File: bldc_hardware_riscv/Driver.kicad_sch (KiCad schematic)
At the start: 95 parts, among them Q1 Q_NMOS_GDS, Q2 Q_NMOS_GDS, Q3 Q_NMOS_GDS, Q4 Q_NMOS_GDS, Q5 Q_NMOS_GDS, Q6 Q_NMOS_GDS, U101 MAX9919, U102 MAX9919, U103 MAX9919, U2 XL1509-3.3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

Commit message: First release to PCB manufacture
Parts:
- U101, U102, U103: value MAX9919 -> (none); footprint BLDC_Library:HSOP-8-1EP_3.9x4.9mm_P1.27mm_EP2.3x2.3mm -> (none)
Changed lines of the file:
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@@
       (effects (font (size 1.27 1.27)) (justify left))
     )
-    (property "Value" "MAX9919" (id 1) (at 212.09 97.79 0)
-      (effects (font (size 1.27 1.27)) (justify left))
-    )
-    (property "Footprint" "BLDC_Library:HSOP-8-1EP_3.9x4.9mm_P1.27mm_EP2.3x2.3mm" (id 2) (at 203.2 99.695 0)
+    (property "Value" "" (id 1) (at 212.09 97.79 0)
+      (effects (font (size 1.27 1.27)) (justify left))
+    )
+    (property "Footprint" "" (id 2) (at 203.2 99.695 0)
       (effects (font (size 1.27 1.27)) hide)
     )
@@
     (pin "2")
   )
-  (symbol (lib_id "BLDC_Library:MAX9919") (at 205.105 31.115 0) (unit 1)
+  (symbol (lib_name "MAX9919_1") (lib_id "BLDC_Library:MAX9919") (at 205.105 31.115 0) (unit 1)
     (in_bom yes) (on_board yes)
     (property "Reference" "U103" (id 0) (at 212.09 31.75 0)
       (effects (font (size 1.27 1.27)) (justify left))
     )
-    (property "Value" "MAX9919" (id 1) (at 212.09 29.21 0)
-      (effects (font (size 1.27 1.27)) (justify left))
-    )
-    (property "Footprint" "BLDC_Library:HSOP-8-1EP_3.9x4.9mm_P1.27mm_EP2.3x2.3mm" (id 2) (at 203.2 31.115 0)
+    (property "Value" "" (id 1) (at 212.09 29.21 0)
+      (effects (font (size 1.27 1.27)) (justify left))
+    )
+    (property "Footprint" "" (id 2) (at 203.2 31.115 0)
       (effects (font (size 1.27 1.27)) hide)
     )
@@
     (pin "2")
   )
-  (symbol (lib_id "BLDC_Library:MAX9919") (at 205.105 65.405 0) (unit 1)
+  (symbol (lib_name "MAX9919_2") (lib_id "BLDC_Library:MAX9919") (at 205.105 65.405 0) (unit 1)
     (in_bom yes) (on_board yes)
     (property "Reference" "U102" (id 0) (at 212.09 66.04 0)
       (effects (font (size 1.27 1.27)) (justify left))
     )
-    (property "Value" "MAX9919" (id 1) (at 212.09 63.5 0)
-      (effects (font (size 1.27 1.27)) (justify left))
-    )
-    (property "Footprint" "BLDC_Library:HSOP-8-1EP_3.9x4.9mm_P1.27mm_EP2.3x2.3mm" (id 2) (at 203.2 65.405 0)
-      (effects (font (size 1.27 1.27)) hide)
-    )
+    (property "Value" "" (id 1) (at 212.09 63.5 0)
+      (effects (font (size 1.27 1.27)) (justify left))
+    )
+    (property "Footprint" "" (id 2) (at 203.2 65.405 0)
+      (effects (font (size 1.27 1.27)) hide)
+    )

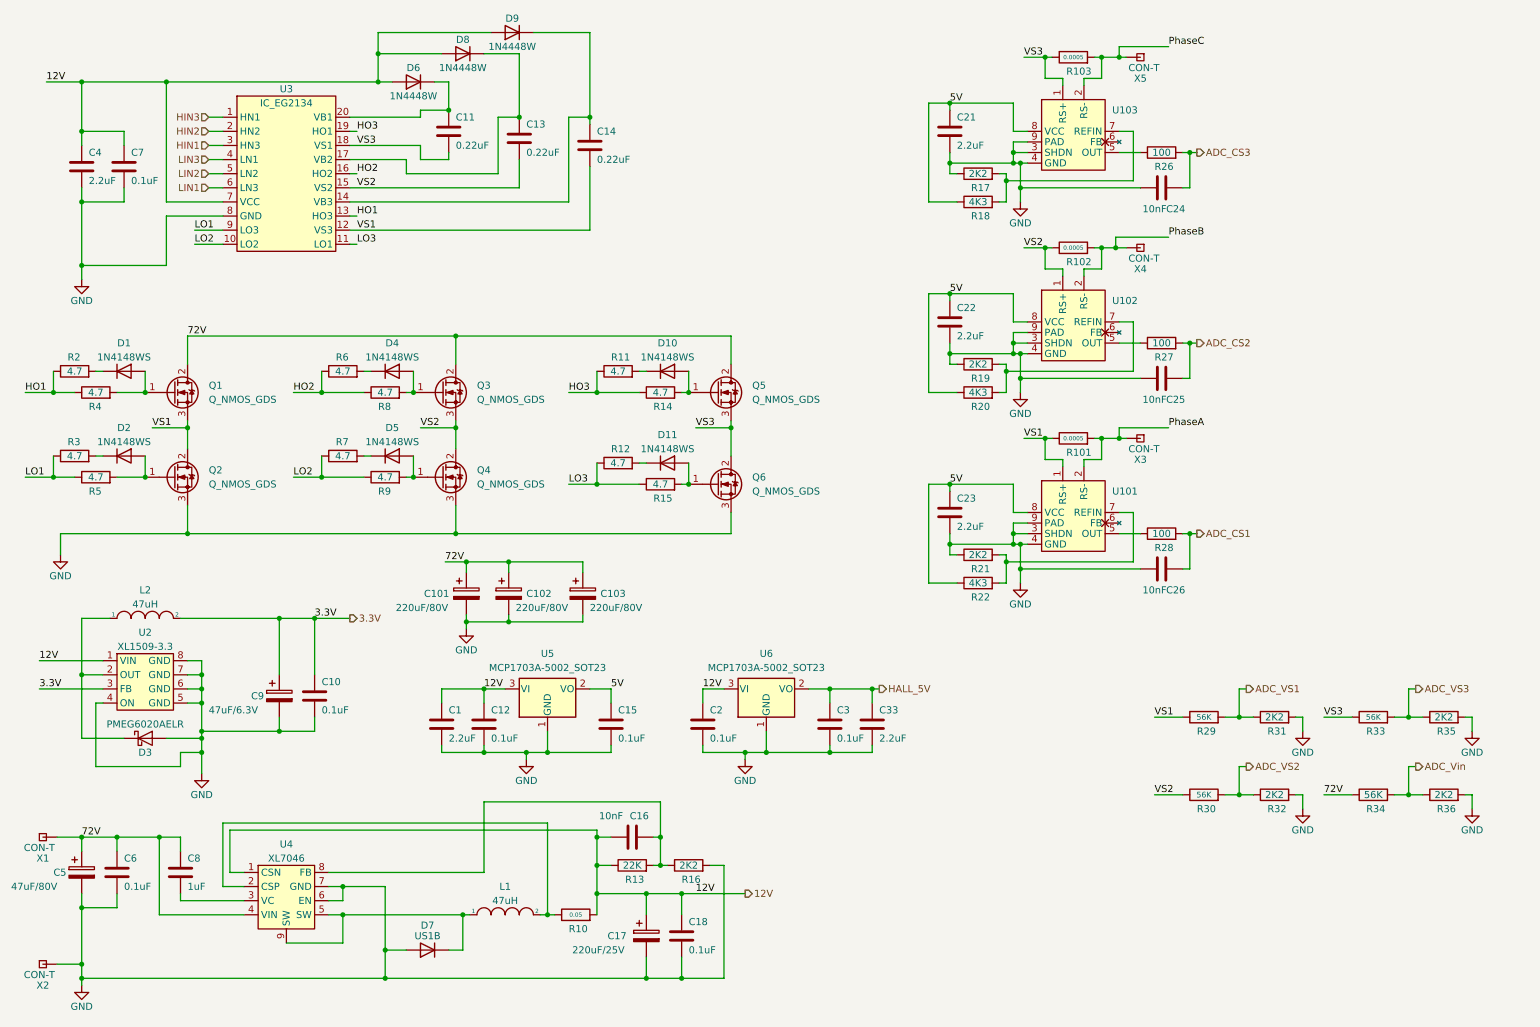
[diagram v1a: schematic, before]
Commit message: fix resistor/inductor/capacitor parameters, add boot button, add 120Ohm CAN bus load resistor.
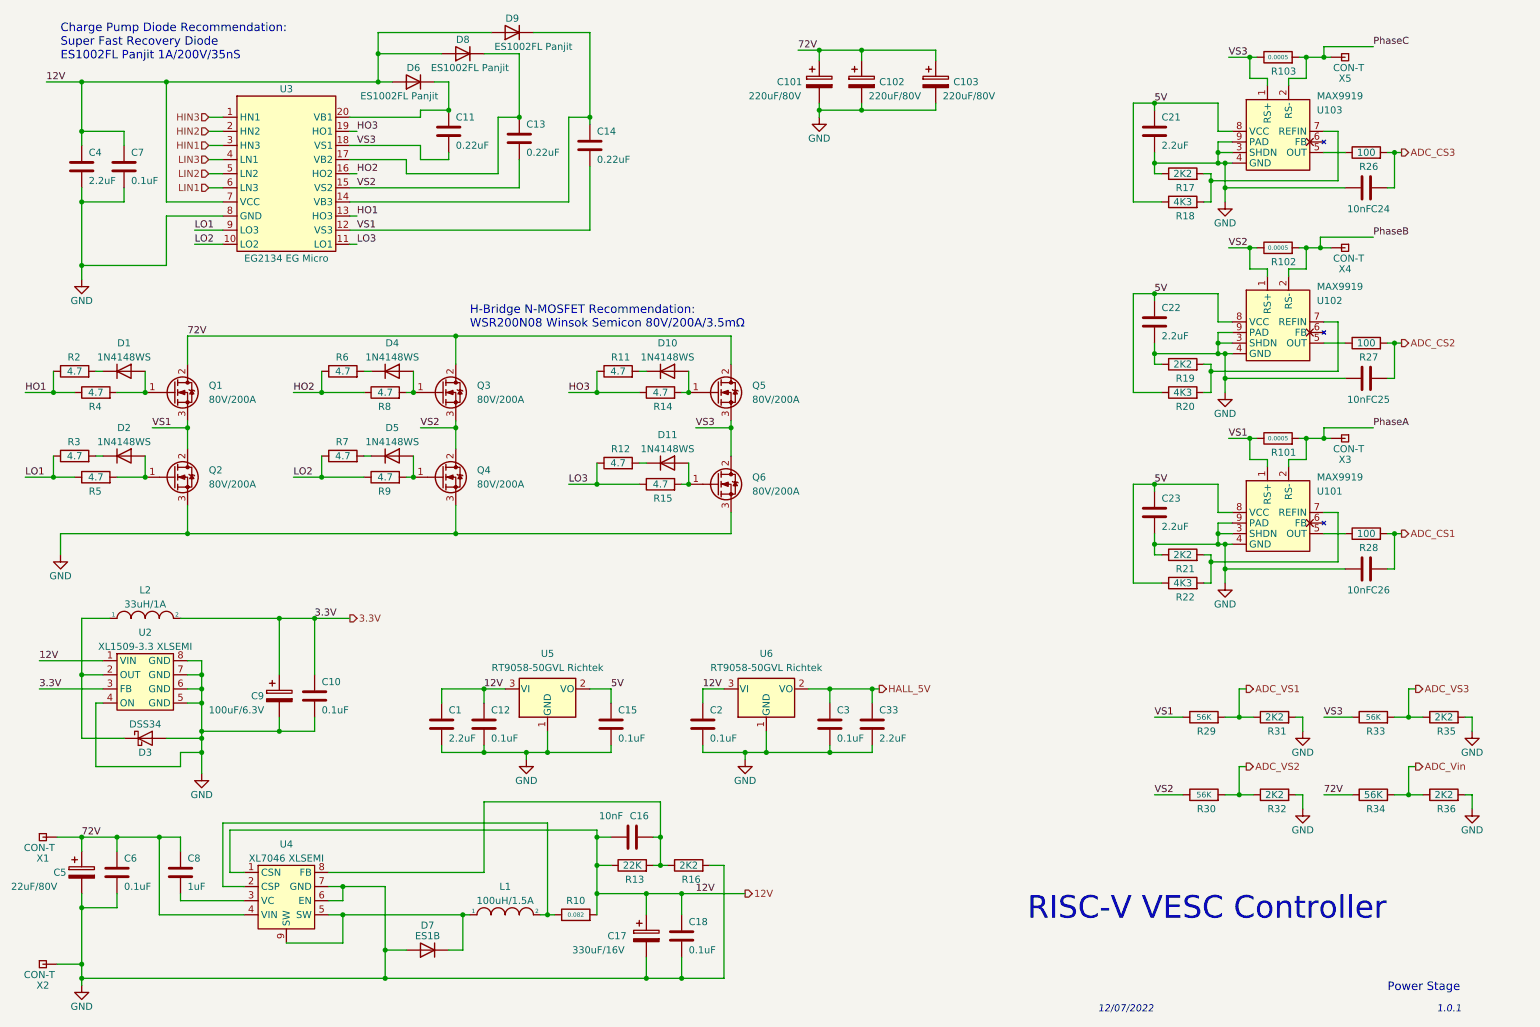
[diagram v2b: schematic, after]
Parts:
- C17: value 220uF/25V -> 330uF/16V
- C5: value 47uF/80V -> 22uF/80V
- C9: value 47uF/6.3V -> 100uF/6.3V
- D3: value PMEG6020AELR -> DSS34
- D6, D8, D9: value 1N4448W -> ES1002FL Panjit; footprint Diode_SMD:D_SOD-123 -> Diode_SMD:D_SOD-123F
- D7: value US1B -> ES1B
- L1: value 47uH -> 100uH/1.5A
- L2: value 47uH -> 33uH/1A
- Q1, Q2, Q3, Q4, Q5, Q6: value Q_NMOS_GDS -> 80V/200A
- R10: value 0.05 -> 0.082
- U101, U102, U103: value (none) -> MAX9919; footprint (none) -> BLDC_Library:HSOP-8-1EP_3.9x4.9mm_P1.27mm_EP2.3x2.3mm
- U2: value XL1509-3.3 -> XL1509-3.3 XLSEMI
- U3: value IC_EG2134 -> EG2134 EG Micro
- U4: value XL7046 -> XL7046 XLSEMI
- U5, U6: value MCP1703A-5002_SOT23 -> RT9058-50GVL Richtek
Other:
- note added: "1.0.1"
- note added: "12/07/2022"
- note added: "Charge Pump Diode Recommendation: Super Fast Recovery Diode ES1002FL Panjit 1A/200V/35nS"
- note added: "H-Bridge N-MOSFET Recommendation: WSR200N08 Winsok Semicon 80V/200A/3.5mΩ"
- note added: "Power Stage"
- note added: "RISC-V VESC Controller"
- moved on the sheet: C101, C102, C103, C21, C22, C23, C24, C25, C26, R101, R102, R103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
